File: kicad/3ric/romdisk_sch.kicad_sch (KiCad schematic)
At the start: 44 parts, among them J2_DECODER_1 74LS154

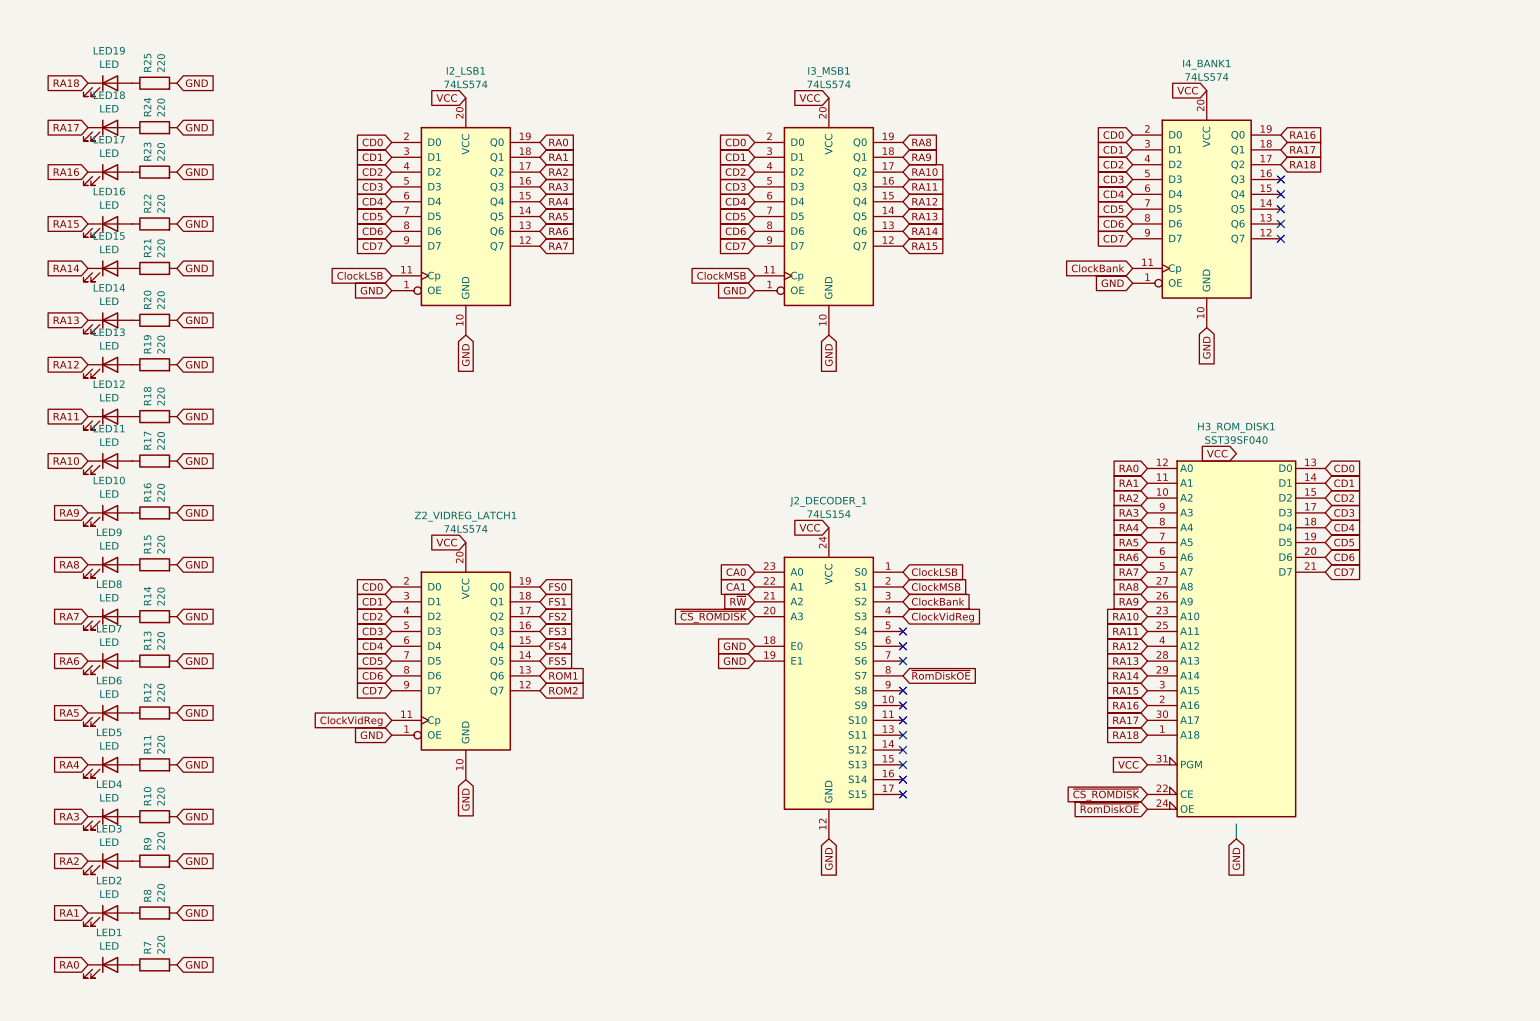
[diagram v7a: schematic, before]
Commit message: updated schematics and PCB PNG of the breadboard layout
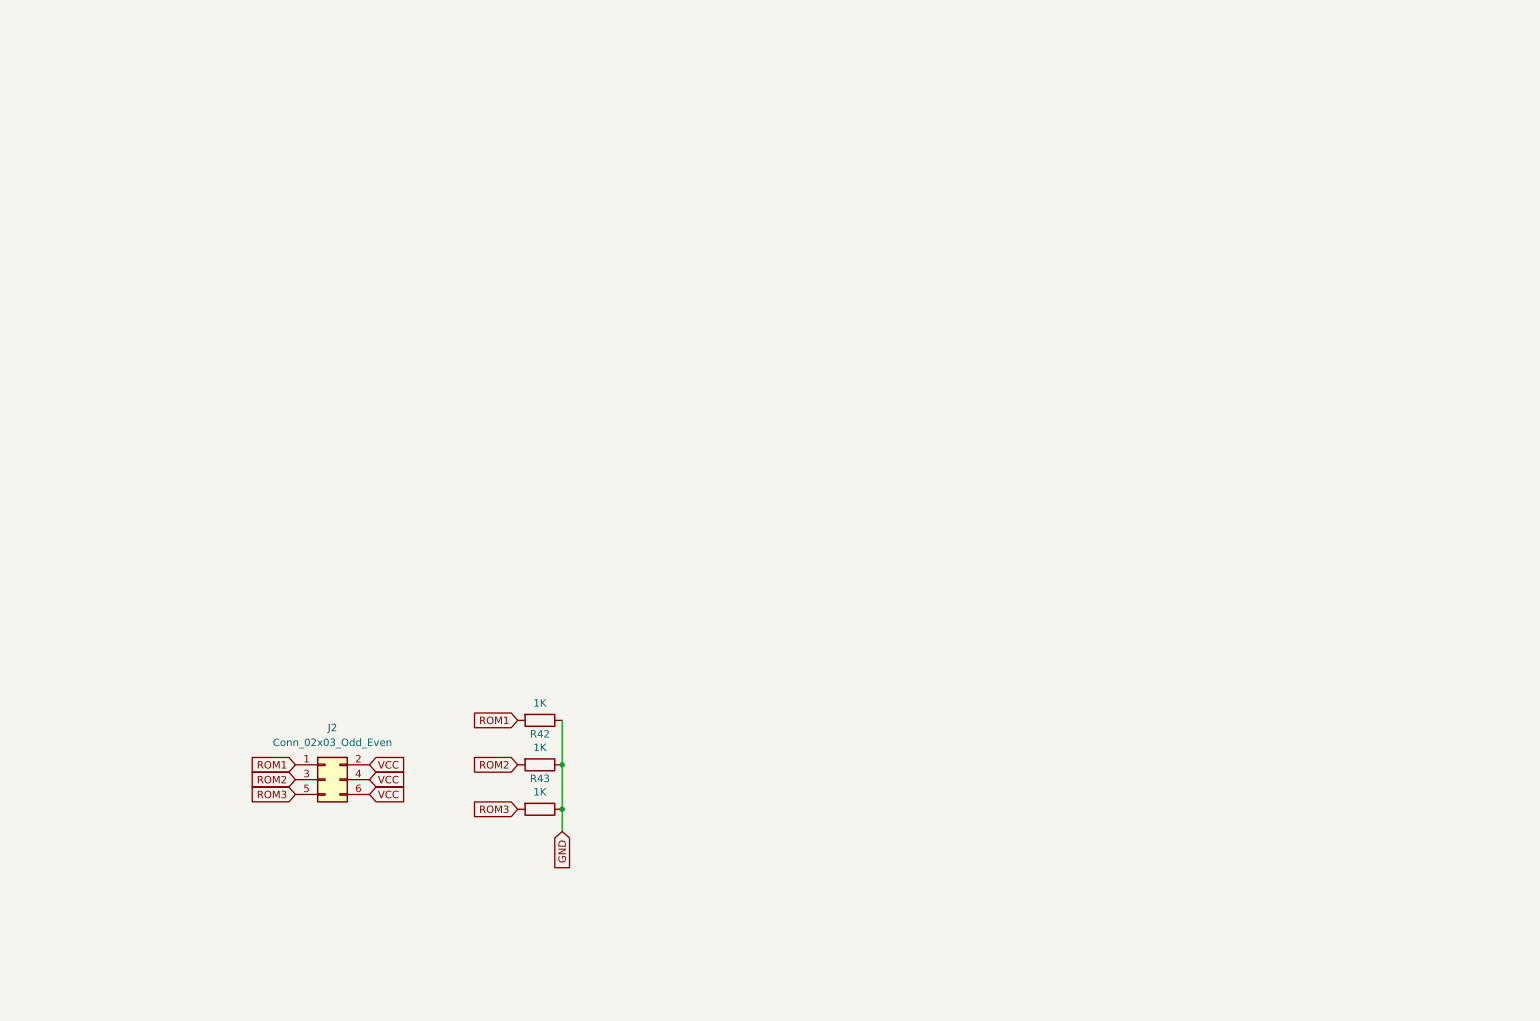
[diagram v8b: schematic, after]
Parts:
- removed H3_ROM_DISK1: SST39SF040, Package_DIP:DIP-32_W15.24mm_Socket, symbol Memory_Flash:SST39SF040
- removed I2_LSB1, I3_MSB1, I4_BANK1, Z2_VIDREG_LATCH1: 74LS574, Package_DIP:DIP-20_W7.62mm_Socket, symbol 74xx:74LS574
- removed J2_DECODER_1: 74LS154, Package_DIP:DIP-24_W15.24mm_Socket, symbol 74xx:74LS154
- removed LED1, LED10, LED11, LED12, LED13, LED14, LED15, LED16, LED17, LED18, LED19, LED2, LED3, LED4, LED5, LED6, LED7, LED8, LED9: LED, LED_THT:LED_D3.0mm, symbol Device:LED
- removed R10, R11, R12, R13, R14, R15, R16, R17, R18, R19, R20, R21, R22, R23, R24, R25, R7, R8, R9: 220, Resistor_THT:R_Axial_DIN0207_L6.3mm_D2.5mm_P7.62mm_Horizontal, symbol Device:R
- added J2: Conn_02x03_Odd_Even, Connector_PinHeader_2.54mm:PinHeader_2x03_P2.54mm_Vertical, symbol Connector_Generic:Conn_02x03_Odd_Even
- added R41, R42, R43: 1K, Resistor_SMD:R_0402_1005Metric_Pad0.72x0.64mm_HandSolder, symbol Device:R
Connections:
- net GND: now also R41.1, R42.1, R43.1
- net ROM1: now also J2.1 (Pin_1), R41.2
- net ROM2: now also J2.3 (Pin_3), R42.2
- net VCC: now also J2.2 (Pin_2), J2.4 (Pin_4), J2.6 (Pin_6)
- new net ROM3: J2.5 (Pin_5), R43.2
- no-connect marks 16 -> 0
